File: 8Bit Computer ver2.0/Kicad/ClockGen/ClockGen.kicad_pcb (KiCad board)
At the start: 2 copper layers, 9 parts, among them IC1 SN74LVC1GU04DCKR, IC2 SN74LVC1G14DBVR, Y1 8MHz

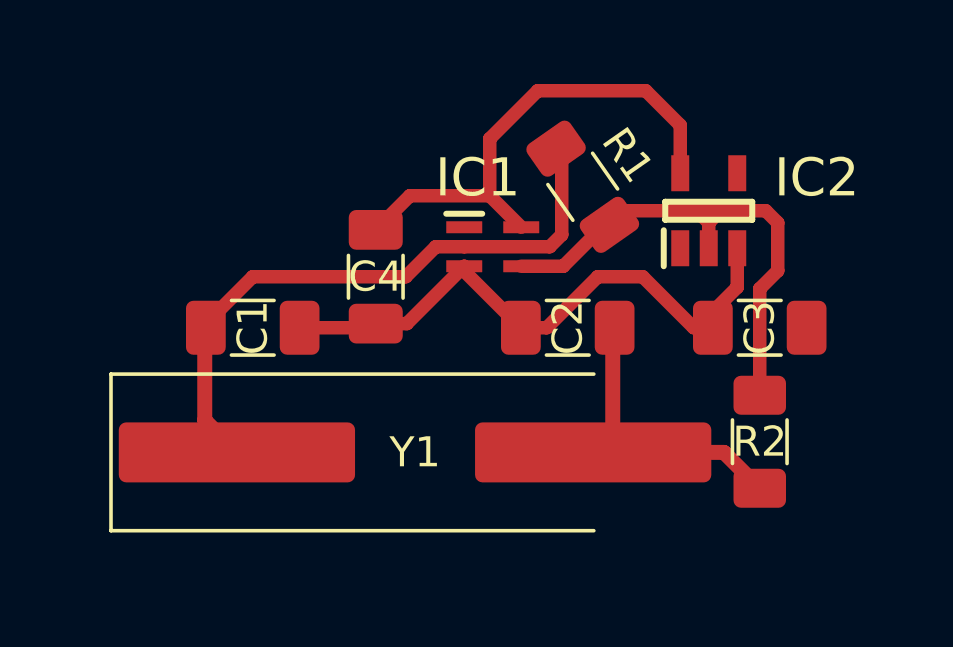
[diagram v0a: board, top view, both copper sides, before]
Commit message: Kicad, folders
Kicad:
added Computer Schematic pdf of the module version
added Clock Gen pdf Schemtics and PCB
folders:
changed old Computer versions to OLD_
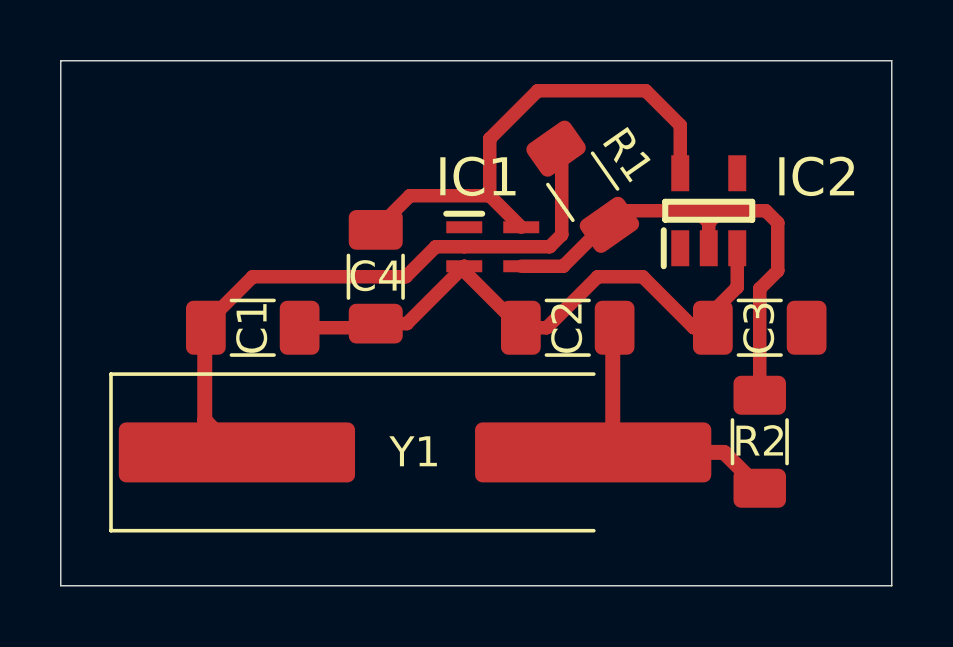
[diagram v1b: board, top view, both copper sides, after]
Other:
- board outline added: 27.7 x 17.5 mm
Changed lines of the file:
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@@
 			(pdf_back_fp_property_popups yes)
 			(pdf_metadata yes)
-			(pdf_single_document no)
+			(pdf_single_document yes)
 			(dxfpolygonmode yes)
 			(dxfimperialunits yes)
@@
 			(crossoutdnponfab yes)
 			(subtractmaskfromsilk no)
-			(outputformat 1)
+			(outputformat 4)
 			(mirror no)
-			(drillshape 1)
+			(drillshape 0)
 			(scaleselection 1)
 			(outputdirectory "")
@@
 		)
 	)
+	(gr_rect
+		(start 99 54.7)
+		(end 126.7 72.2)
+		(stroke
+			(width 0.05)
+			(type default)
+		)
+		(fill no)
+		(layer "Edge.Cuts")
+	)
 	(segment

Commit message: Kicad, parts
parts:
added Mux 4:1 for CLK
added LM555
Kicad:
added some Diodes for Flash disable
fixed wrong routing of flag register
fixed wrong routing of STC STF in INC/AddS
LM555 circuit for 1Hz to 100Hz
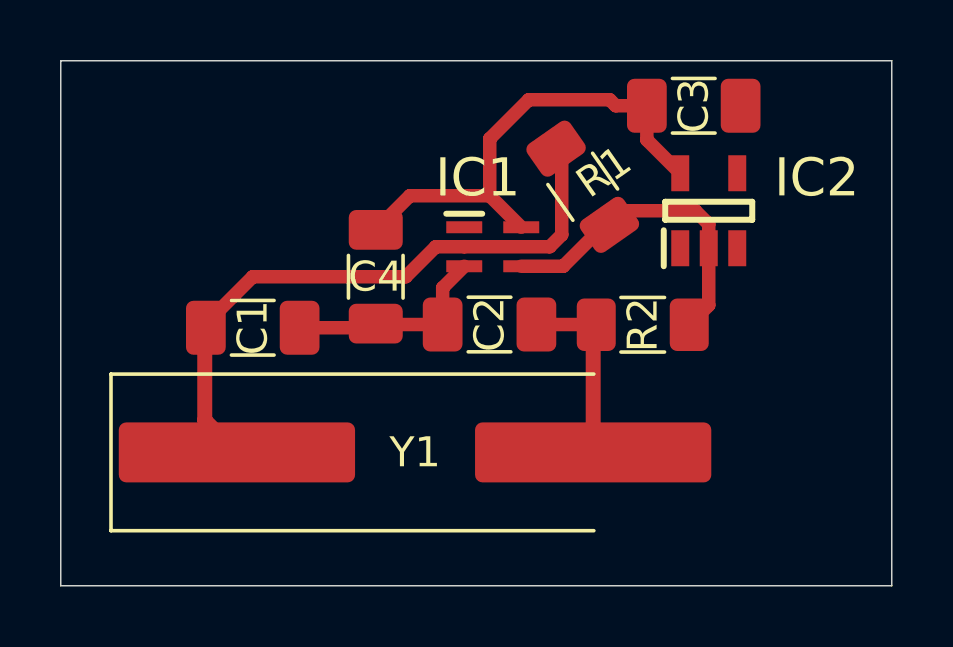
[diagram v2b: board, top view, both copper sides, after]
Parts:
- moved C3 7.72 mm to (120.1, 56.2), turned to 0 degrees
- moved R2 5.52 mm to (118.4, 63.5), turned to 180 degrees
- moved C2 2.61 mm to (113.3, 63.5)
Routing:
- net GND: track 20.0 -> 7.08 mm
- net Net-(IC1-Y): track 17.5 -> 11.3 mm
- net Net-(C2-Pad1): track 10.5 -> 7.23 mm
- net +5V: track 16.7 -> 16.2 mm
